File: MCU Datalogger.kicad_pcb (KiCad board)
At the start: 2 copper layers, 0 parts

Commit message: Completed placement of footprints
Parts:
- added BT1: Battery, Connector_PinHeader_2.54mm:PinHeader_1x02_P2.54mm_Vertical, F.Cu at (83.8, 74.9)
- added C1: 22pF, Capacitor_SMD:C_0805_2012Metric, F.Cu at (98.1, 77.7)
- added C2: 22pF, Capacitor_SMD:C_0805_2012Metric, F.Cu at (117.9, 45.0)
- added C3: 0.1 uF, Capacitor_SMD:C_0805_2012Metric, F.Cu at (101.7, 77.7)
- added C4: 0.1 uF, Capacitor_SMD:C_0805_2012Metric, F.Cu at (114.8, 77.2)
- added C5: 100nF, Capacitor_SMD:C_0805_2012Metric, F.Cu at (105.2, 77.7)
- added D1: LED, LED_SMD:LED_0805_2012Metric, F.Cu at (117.2, 63.0)
- added D2: LED, LED_SMD:LED_0805_2012Metric, F.Cu at (121.0, 63.0)
- added H1: MountingHole, MountingHole:MountingHole_2.1mm, F.Cu at (83.8, 59.7)
- added H2: MountingHole, MountingHole:MountingHole_2.1mm, F.Cu at (83.8, 82.5)
- added H3: MountingHole, MountingHole:MountingHole_2.1mm, F.Cu at (128.3, 82.5)
- added H4: MountingHole, MountingHole:MountingHole_2.1mm, F.Cu at (128.3, 59.7)
- added J1: Conn_01x04_Pin, Connector_PinHeader_2.54mm:PinHeader_1x04_P2.54mm_Vertical, F.Cu at (116.3, 58.4)
- added J2: Conn_01x04_Pin, Connector_PinHeader_2.54mm:PinHeader_1x04_P2.54mm_Vertical, F.Cu at (115.6, 83.8)
- added J3: Conn_01x09_Pin, Connector_PinHeader_2.54mm:PinHeader_1x09_P2.54mm_Vertical, F.Cu at (88.9, 83.8)
- added J4: Conn_02x03_Odd_Even, Connector_PinHeader_2.54mm:PinHeader_2x03_P2.54mm_Vertical, F.Cu at (125.7, 64.8)
- added R1: 4.7K, Resistor_SMD:R_0805_2012Metric, F.Cu at (99.1, 68.0)
- added R2: 4.7K, Resistor_SMD:R_0805_2012Metric, F.Cu at (99.1, 71.7)
- added R3: 10K, Resistor_SMD:R_0805_2012Metric, F.Cu at (131.2, 36.8)
- added R4: 330, Resistor_SMD:R_0805_2012Metric, F.Cu at (114.9, 65.7)
- added R5: 330, Resistor_SMD:R_0805_2012Metric, F.Cu at (114.9, 68.7)
- added R6: 10K, Resistor_SMD:R_0805_2012Metric, F.Cu at (114.9, 71.6)
- added R7: 10K, Resistor_SMD:R_0805_2012Metric, F.Cu at (114.9, 74.6)
- added U1: 24LC1025, Package_SO:SOIC-8_5.3x5.3mm_P1.27mm, F.Cu at (91.9, 60.5)
- added U2: 24LC1025, Package_SO:SOIC-8_5.3x5.3mm_P1.27mm, F.Cu at (91.9, 68.1)
- added U3: DS1337S_, DS1337S:SOIC127P600X175-8N, F.Cu at (91.4, 75.7)
- added U4: ATMEGA328P-AU, ATMEGA328P-AU:QFP80P900X900X120-32N, F.Cu at (105.7, 63.0)
- added Y1: 16MHz, Crystal:Crystal_SMD_5032-2Pin_5.0x3.2mm_HandSoldering, F.Cu at (83.8, 67.3)
- added Y2: 32.768 KHz, Crystal:Crystal_SMD_5032-2Pin_5.0x3.2mm_HandSoldering, F.Cu at (106.1, 72.1)
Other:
- board outline added: 49.5 x 29.2 mm

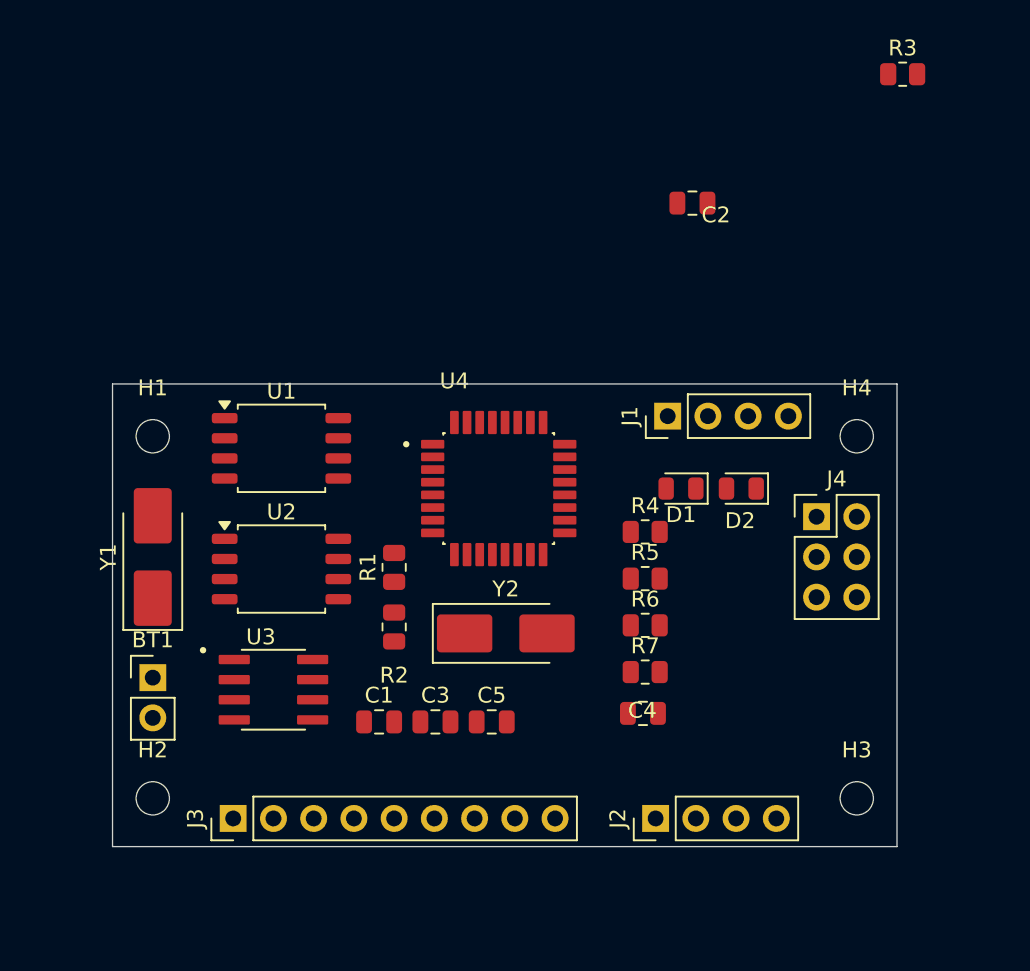
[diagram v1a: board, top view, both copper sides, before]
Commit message: Completed the routing of the board
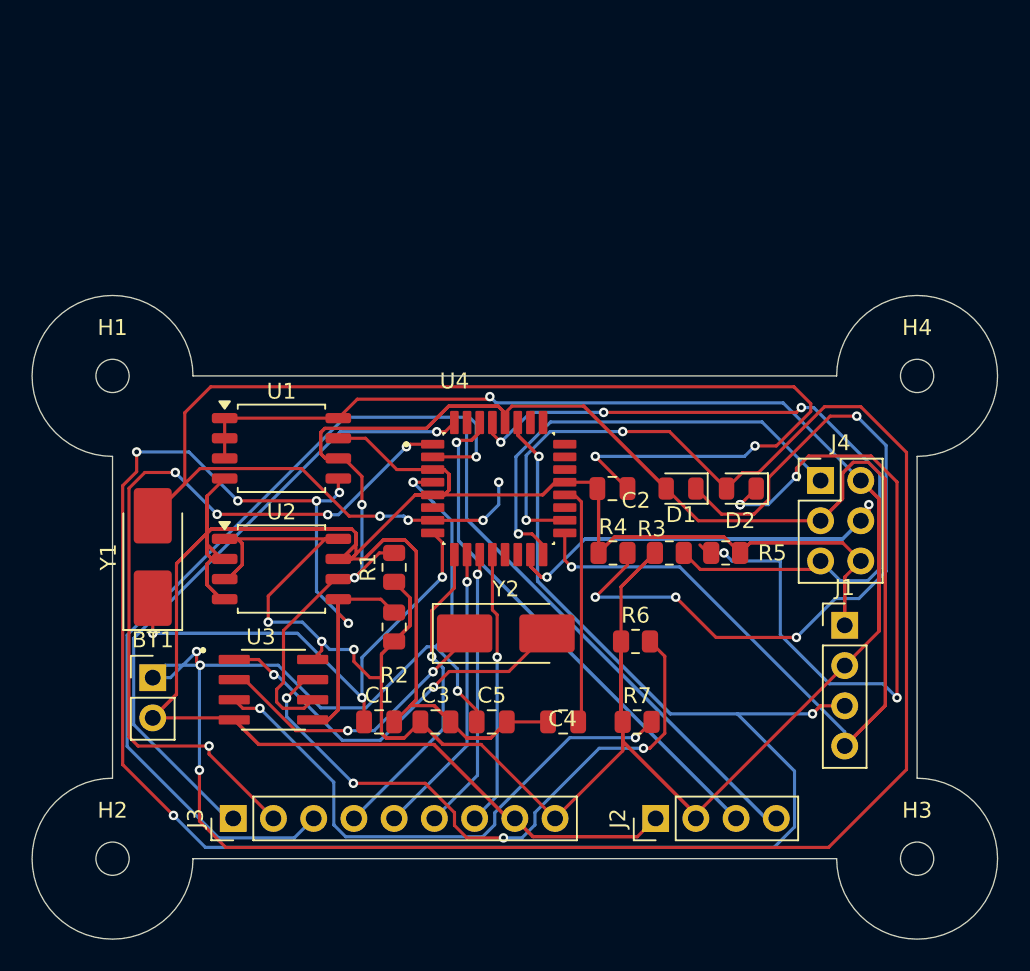
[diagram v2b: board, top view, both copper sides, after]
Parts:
- moved R3 33.6 mm to (116.4, 67.1)
- moved C2 18.7 mm to (112.8, 63.0)
- moved J1 17.3 mm to (127.5, 71.6), turned to 0 degrees
- moved H3 5.39 mm to (132.1, 86.4)
- moved H4 5.39 mm to (132.1, 55.9)
- moved R5 5.33 mm to (120.0, 67.1)
- moved C4 5.07 mm to (109.7, 77.7)
- moved H2 4.58 mm to (81.3, 86.4)
- moved H1 4.58 mm to (81.3, 55.9)
- moved R7 3.19 mm to (114.4, 77.7)
- moved R4 2.43 mm to (112.9, 67.1)
- moved J4 2.30 mm to (126.0, 62.5)
- moved R6 1.19 mm to (114.3, 72.6)
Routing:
- net GND: track 0.00 -> 257.1 mm
- net /VCC: track 0.00 -> 201.0 mm, vias 0 -> 4
- net /SDA: track 0.00 -> 185.1 mm, vias 0 -> 8
- net Net-(BT1-+): track 0.00 -> 157.5 mm, vias 0 -> 7
- net /SCK: track 0.00 -> 157.5 mm, vias 0 -> 3
- net Net-(U4-PB6): track 0.00 -> 92.4 mm, vias 0 -> 6
- net /TX: track 0.00 -> 61.4 mm
- net /RX: track 0.00 -> 60.1 mm, vias 0 -> 1
- net /D4: track 0.00 -> 54.4 mm, vias 0 -> 1
- net /D3: track 0.00 -> 49.8 mm, vias 0 -> 5
- net Net-(D1-K): track 0.00 -> 49.5 mm, vias 0 -> 4
- net /RESET: track 0.00 -> 47.9 mm, vias 0 -> 3
- net Net-(D2-K): track 0.00 -> 46.4 mm, vias 0 -> 5
- net /MOSI: track 0.00 -> 44.3 mm, vias 0 -> 2
- net Net-(U4-PB7): track 0.00 -> 43.0 mm, vias 0 -> 3
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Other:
- board size 49.5 x 29.2 mm -> 61 x 40.6 mm
